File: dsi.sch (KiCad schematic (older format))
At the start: 18 parts, among them J1201 Touch, J1202 LCD, Q1201 2SK3018, Q1202 2SK3018

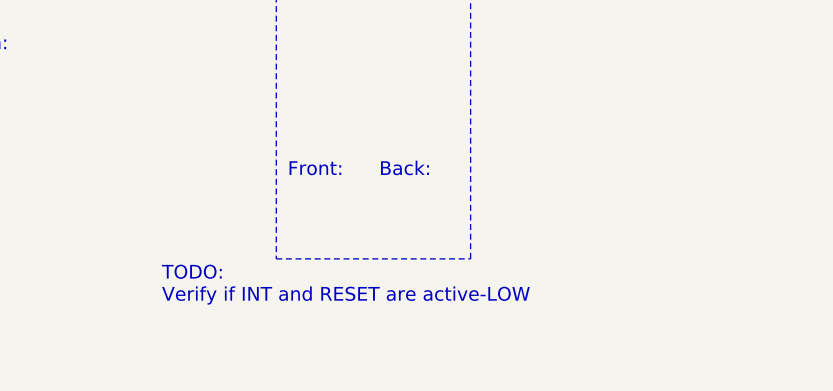
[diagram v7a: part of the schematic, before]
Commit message: Replace the AP22800 load switch with the P-channel AP22814 load switch IC due to its reverse current & over current protection capability, add level shifter circuit to the WWAN's DPR signal
Reverse current is no longer an issue with the load switches. One more obvious "TODO" for the schematic left which is to simply place several 100nF bypass caps on the 5V_P, 3V3_P, and 1V8_P rails (investigate how EmCraft is placing these in their layout).
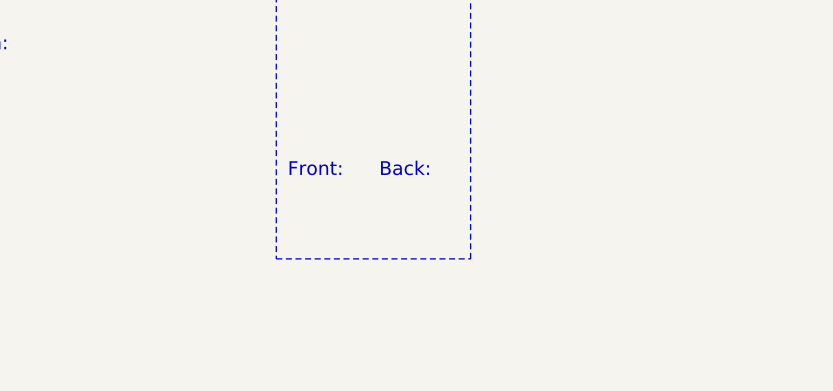
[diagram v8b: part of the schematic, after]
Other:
- note removed: "TODO:\nVerify if INT and RESET are active-LOW"
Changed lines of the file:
@@
 Note:\nNo power-up sequence is\ngiven in the spec sheet
 $Comp
-L 3V3_P #PWR0185
+L 3V3_P #PWR0186
 U 1 1 5AEA3227
 P 4000 3150
-F 0 "#PWR0185" H 4000 3000 50  0001 C CNN
+F 0 "#PWR0186" H 4000 3000 50  0001 C CNN
 F 1 "3V3_P" H 4000 3290 50  0000 C CNN
 F 2 "" H 4000 3150 50  0001 C CNN
@@
 $EndComp
 $Comp
-L 3V3_P #PWR0186
+L 3V3_P #PWR0187
 U 1 1 5AEA329B
 P 2100 3250
-F 0 "#PWR0186" H 2100 3100 50  0001 C CNN
+F 0 "#PWR0187" H 2100 3100 50  0001 C CNN
 F 1 "3V3_P" H 2100 3390 50  0000 C CNN
 F 2 "" H 2100 3250 50  0001 C CNN
@@
 $EndComp
 $Comp
-L 1V8_P #PWR0187
+L 1V8_P #PWR0188
 U 1 1 5AEDE2F3
 P 2700 3250
-F 0 "#PWR0187" H 2700 3100 50  0001 C CNN
+F 0 "#PWR0188" H 2700 3100 50  0001 C CNN
 F 1 "1V8_P" H 2700 3390 50  0000 C CNN
 F 2 "" H 2700 3250 50  0001 C CNN
@@
 $EndComp
 $Comp
-L 1V8_P #PWR0188
+L 1V8_P #PWR0189
 U 1 1 5B300B10
 P 4850 3150
-F 0 "#PWR0188" H 4850 3000 50  0001 C CNN
+F 0 "#PWR0189" H 4850 3000 50  0001 C CNN
 F 1 "1V8_P" H 4850 3290 50  0000 C CNN
 F 2 "" H 4850 3150 50  0001 C CNN
@@
 $EndComp
 $Comp
-L GND #PWR0189
+L GND #PWR0190
 U 1 1 5B314AC6
 P 9400 5100
-F 0 "#PWR0189" H 9400 4850 50  0001 C CNN
+F 0 "#PWR0190" H 9400 4850 50  0001 C CNN
 F 1 "GND" H 9400 4950 50  0000 C CNN
 F 2 "" H 9400 5100 50  0001 C CNN
@@
 NoConn ~ 9450 4850
 $Comp
-L 22V4_P #PWR0190
+L 22V4_P #PWR0191
 U 1 1 5B3239F0
 P 8700 5000
-F 0 "#PWR0190" H 8700 4850 50  0001 C CNN
+F 0 "#PWR0191" H 8700 4850 50  0001 C CNN
 F 1 "22V4_P" H 8700 5140 50  0000 C CNN
 F 2 "" H 8700 5000 50  0001 C CNN
@@
 NoConn ~ 9450 2950
 $Comp
-L 1V8_P #PWR0191
+L 1V8_P #PWR0192
 U 1 1 5B328FC1
 P 7900 2400
-F 0 "#PWR0191" H 7900 2250 50  0001 C CNN
+F 0 "#PWR0192" H 7900 2250 50  0001 C CNN
 F 1 "1V8_P" H 7900 2540 50  0000 C CNN
 F 2 "" H 7900 2400 50  0001 C CNN
@@
 $EndComp
 $Comp
-L GND #PWR0192
+L GND #PWR0193
 U 1 1 5B32A2F2
 P 7900 3000
-F 0 "#PWR0192" H 7900 2750 50  0001 C CNN
+F 0 "#PWR0193" H 7900 2750 50  0001 C CNN
 F 1 "GND" H 7900 2850 50  0000 C CNN
 F 2 "" H 7900 3000 50  0001 C CNN
@@
 	9350 4550 9450 4550
 $Comp
-L 2V8_P #PWR0193
+L 2V8_P #PWR0194
 U 1 1 5B3FFD6E
 P 8700 2400
-F 0 "#PWR0193" H 8700 2250 50  0001 C CNN
+F 0 "#PWR0194" H 8700 2250 50  0001 C CNN
 F 1 "2V8_P" H 8700 2540 50  0000 C CNN
 F 2 "" H 8700 2400 50  0001 C CNN
@@
 $EndComp
 $Comp
-L GND #PWR0194
+L GND #PWR0195
 U 1 1 5B3FFE19
 P 8700 2950
-F 0 "#PWR0194" H 8700 2700 50  0001 C CNN
+F 0 "#PWR0195" H 8700 2700 50  0001 C CNN
 F 1 "GND" H 8700 2800 50  0000 C CNN
 F 2 "" H 8700 2950 50  0001 C CNN
@@
 	5900 3500 6000 3500
 $Comp
-L GND #PWR0195
+L GND #PWR0196
 U 1 1 5B449295
 P 5950 3950
-F 0 "#PWR0195" H 5950 3700 50  0001 C CNN
+F 0 "#PWR0196" H 5950 3700 50  0001 C CNN
 F 1 "GND" H 5950 3800 50  0000 C CNN
 F 2 "" H 5950 3950 50  0001 C CNN
@@
 	5950 2700 5950 3800
 $Comp
-L 2V8_P #PWR0196
+L 2V8_P #PWR0197
 U 1 1 5B449772
 P 5950 2700
-F 0 "#PWR0196" H 5950 2550 50  0001 C CNN
+F 0 "#PWR0197" H 5950 2550 50  0001 C CNN
 F 1 "2V8_P" H 5950 2840 50  0000 C CNN
 F 2 "" H 5950 2700 50  0001 C CNN
@@
 $EndComp
 $Comp
-L GND #PWR0197
+L GND #PWR0198
 U 1 1 5B44A063
 P 5800 3150
-F 0 "#PWR0197" H 5800 2900 50  0001 C CNN
+F 0 "#PWR0198" H 5800 2900 50  0001 C CNN
 F 1 "GND" H 5800 3000 50  0000 C CNN
 F 2 "" H 5800 3150 50  0001 C CNN
@@
 $EndComp
 $Comp
-L GND #PWR0198
+L GND #PWR0199
 U 1 1 5B45292C
 P 8700 5600
-F 0 "#PWR0198" H 8700 5350 50  0001 C CNN
+F 0 "#PWR0199" H 8700 5350 50  0001 C CNN
 F 1 "GND" H 8700 5450 50  0000 C CNN
 F 2 "" H 8700 5600 50  0001 C CNN
@@
 Wire Notes Line
 	10650 4550 9950 4550
-Text Notes 4300 5550 0    60   ~ 0
-TODO:\nVerify if INT and RESET are active-LOW
 Text Notes 8000 4700 0    60   ~ 0
 100Ω Differential Impedance
